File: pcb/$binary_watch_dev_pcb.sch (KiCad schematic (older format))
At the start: 67 parts, among them K1 PWR_SELECT, M1 MNT, M2 MNT, M3 MNT, M4 MNT, P1 ISP, P2 USB-MICRO-B, P3 LED_ISENSE, P7 MCU_ISENSE, P8 TST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

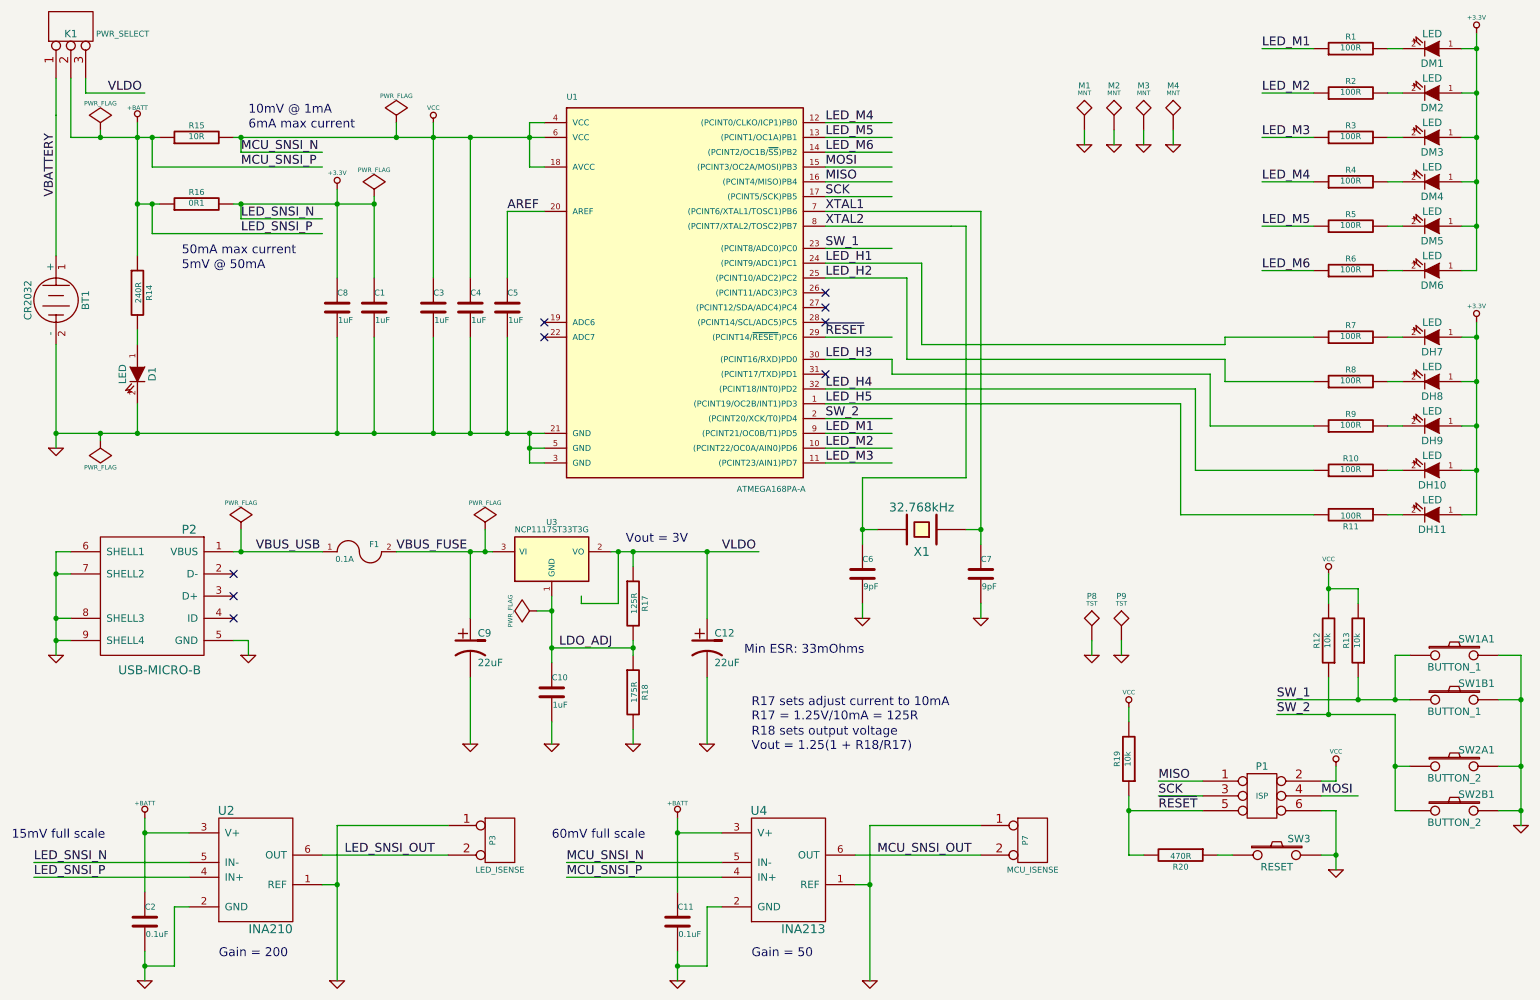
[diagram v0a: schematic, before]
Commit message: Move to 5x5 board for cost
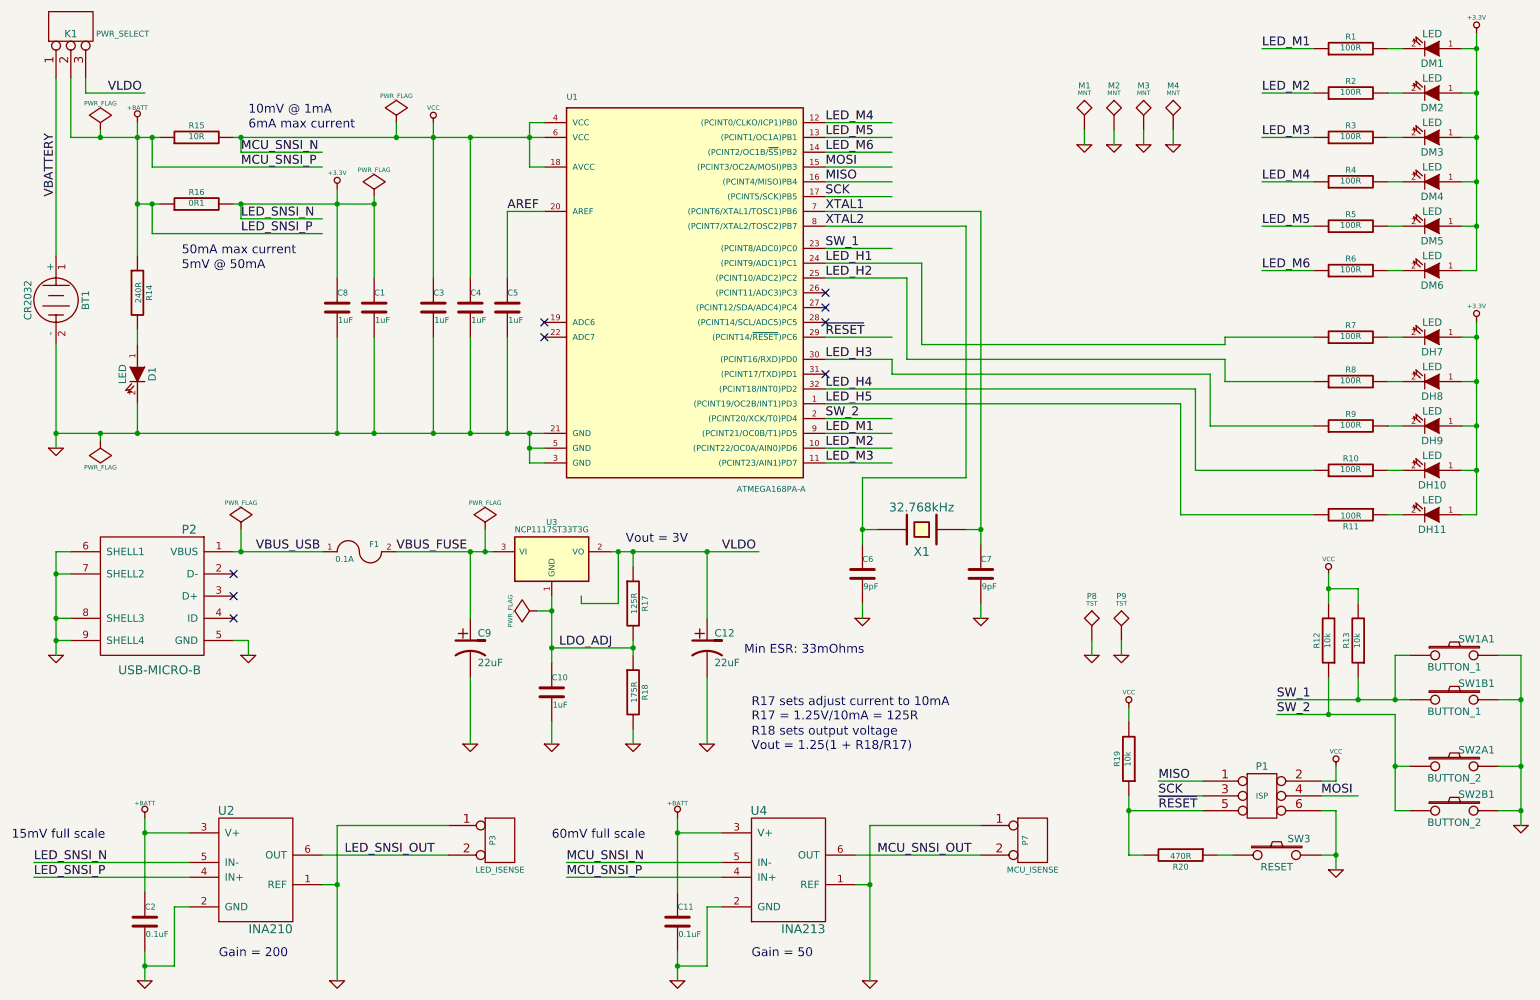
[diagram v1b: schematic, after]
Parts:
- C6, C7: footprint Capacitors_SMD:C_0603_HandSoldering -> Capacitors_SMD:C_0402
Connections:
- wire segments 269 -> 200
